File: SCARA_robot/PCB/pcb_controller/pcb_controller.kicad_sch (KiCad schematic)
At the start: 41 parts, among them IC1 LD1117-3.3V-SOT223, J1 Barrel_Jack_Switch, J10 interface, J11 Conn_01x07_Socket, J12 Encoder_A, J13 Encoder_B, J14 Encoder_C, J2 Conn_01x04_Pin_STEPPER_A, J3 interface, J4 power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

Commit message: schematic ready
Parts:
- added A2, A3: Pololu_Breakout_DRV8825, Module:Pololu_Breakout-16_15.2x20.3mm, symbol Driver_Motor:Pololu_Breakout_DRV8825
- added J15: Conn_01x04_Pin_STEPPER_B, Connector_JST:JST_XH_B4B-XH-AM_1x04_P2.50mm_Vertical, symbol Connector:Conn_01x04_Pin
- added J16: Conn_01x04_Pin_STEPPER_C, Connector_JST:JST_XH_B4B-XH-AM_1x04_P2.50mm_Vertical, symbol Connector:Conn_01x04_Pin
- added JP4, JP5, JP6: SolderJumper_2_Open, Jumper:SolderJumper-2_P1.3mm_Open_RoundedPad1.0x1.5mm, symbol Jumper:SolderJumper_2_Open
- added SW2, SW3: Microstep mode, Button_Switch_THT:SW_DIP_SPSTx03_Slide_9.78x9.8mm_W7.62mm_P2.54mm, symbol Switch:SW_DIP_x03
- added U3: PCA9548A, symbol modules:1{colon}8_i2c_mux
- JP1, JP2, JP3: footprint (none) -> Jumper:SolderJumper-3_P1.3mm_Open_RoundedPad1.0x1.5mm
- SW1: footprint (none) -> Button_Switch_THT:SW_DIP_SPSTx03_Slide_9.78x9.8mm_W7.62mm_P2.54mm
- U1: footprint PCM_Package_TO_SOT_THT_AKL:TO-220-3_Vertical -> PCM_4ms_Package_TO:TO-220-3_Horizontal
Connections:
- net +12V: now also A2.8 (VMOT), A3.8 (VMOT)
- net +3.3V: now also SW2.1, SW2.2, SW2.3, SW3.1, SW3.2, SW3.3, U3.1 (vin)
- net GNDA: now also A2.1 (GND), A2.7 (GND), A3.1 (GND), A3.7 (GND), U3.2 (gnd), U3.6 (a0), U3.7 (a1), U3.8 (a2)
- net rst_master: now also U2.4 (D2), U3.5 (rst)
- net scl_enA: now also R4.2, U3.13 (sc7); no longer R5.2
- net scl_enB: now also R6.2, U3.15 (sc6); no longer R7.2
- net scl_enC: now also R8.2, U3.17 (sc5); no longer R9.2
- net scl_master: now also R1.2, U2.14 (D22), U3.4 (scl); no longer R2.2
- net sda_enA: now also R5.2, U3.14 (sd7); no longer R4.2
- net sda_enB: now also R7.2, U3.16 (sd6); no longer R6.2
- net sda_enC: now also R9.2, U3.18 (sd5); no longer R8.2
- net sda_master: now also R2.2, U2.11 (D21), U3.3 (sda); no longer R1.2
- net baseM_rst: now reaches U2.15 (D23)
- net baseM_rst: now also A1.13 (~{RST})
- net link2_dir: now reaches U2.21 (D32)
- net link2_dir: now also A3.16 (DIR)
- net link1_dir: now reaches U2.22 (D33)
- net link1_dir: now also A2.16 (DIR)
- net baseM_step: now reaches U2.23 (D25)
- net baseM_step: now also A1.15 (STEP)
- net link1_step: now reaches U2.24 (D26)
- net link1_step: now also A2.15 (STEP)
- net link2_step: now reaches U2.25 (D27)
- net link2_step: now also A3.15 (STEP)
- net baseM_dir: now reaches U2.28 (D13)
- net baseM_dir: now also A1.16 (DIR)
- net link2_rst: now reaches U2.6 (RX2)
- net link2_rst: now also A3.13 (~{RST})
- net link1_rst: now reaches U2.7 (TX2)
- net link1_rst: now also A2.13 (~{RST})
- net at A1.14 (~{SLP}): now also JP4.2 (B)
- net at A1.2 (~{FLT}): now also JP4.1 (A)
- new net: A3.12 (M2), SW3.4
- new net: A3.11 (M1), SW3.5
- new net: A3.10 (M0), SW3.6
- new net: A2.12 (M2), SW2.4
- new net: A2.11 (M1), SW2.5
- new net: A2.10 (M0), SW2.6
- new net: A2.6 (B2), J15.1 (Pin_1)
- new net: A2.5 (B1), J15.2 (Pin_2)
- new net: A2.3 (A2), J15.3 (Pin_3)
- new net: A2.4 (A1), J15.4 (Pin_4)
- new net: A2.2 (~{FLT}), JP5.1 (A)
- new net: A2.14 (~{SLP}), JP5.2 (B)
- new net: A3.2 (~{FLT}), JP6.1 (A)
- new net: A3.14 (~{SLP}), JP6.2 (B)
- new net: A3.6 (B2), J16.1 (Pin_1)
- new net: A3.5 (B1), J16.2 (Pin_2)
- new net: A3.3 (A2), J16.3 (Pin_3)
- new net: A3.4 (A1), J16.4 (Pin_4)
- no-connect marks 5 -> 17
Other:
- moved on the sheet: A1, J2, R1, R10, R2, R4, R5, R6, R7, R8, R9, SW1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

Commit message: schematic ready
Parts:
- removed IC1: LD1117-3.3V-SOT223, PCM_Package_TO_SOT_SMD_AKL:TO-252-2_ThermalVias, symbol PCM_4ms_Regulator:LD1117-3.3V-SOT223
- added U4: LD1117S33TR_SOT223, Package_TO_SOT_SMD:SOT-223-3_TabPin2, symbol Regulator_Linear:LD1117S33TR_SOT223
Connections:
- net +3.3V: now also U4.2 (VO)
- net +5V: now also U4.3 (VI)
- net GNDA: now also U4.1 (GND)
- no-connect marks 17 -> 28
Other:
- moved on the sheet: R4, R5, R6, R7, R8, R9

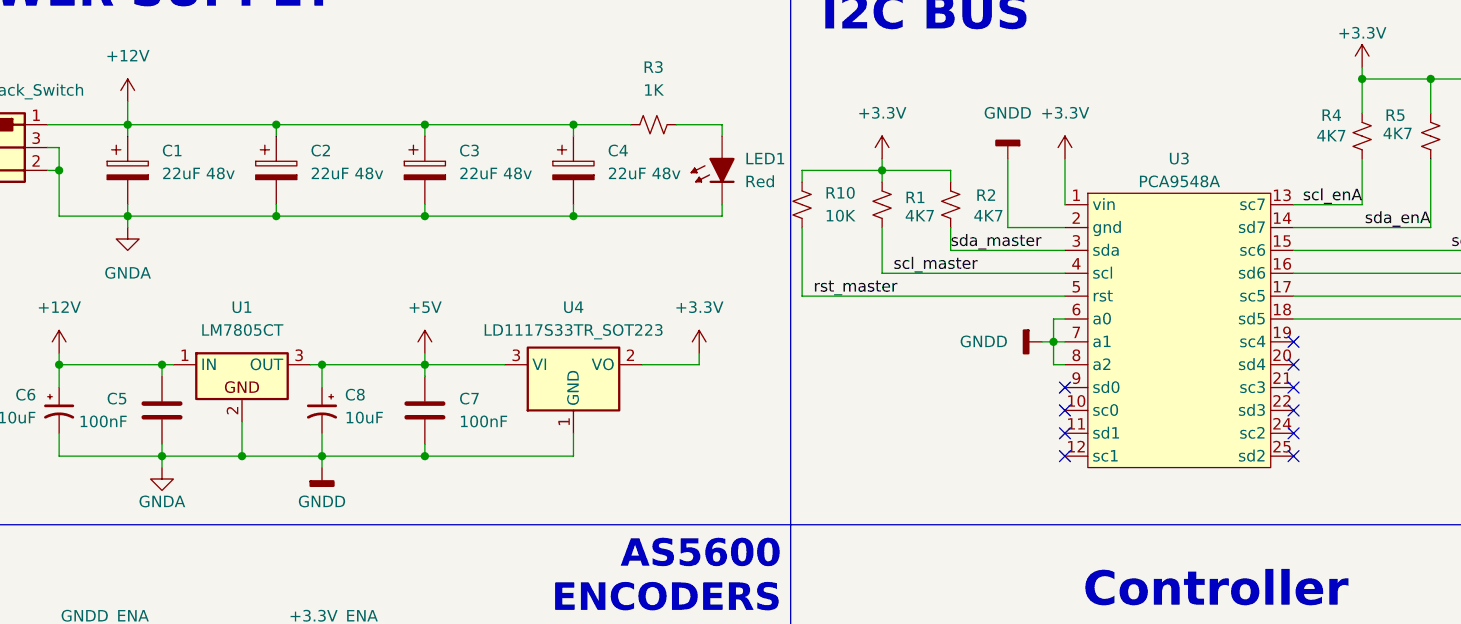
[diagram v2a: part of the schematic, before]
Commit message: schematic and footprints ready
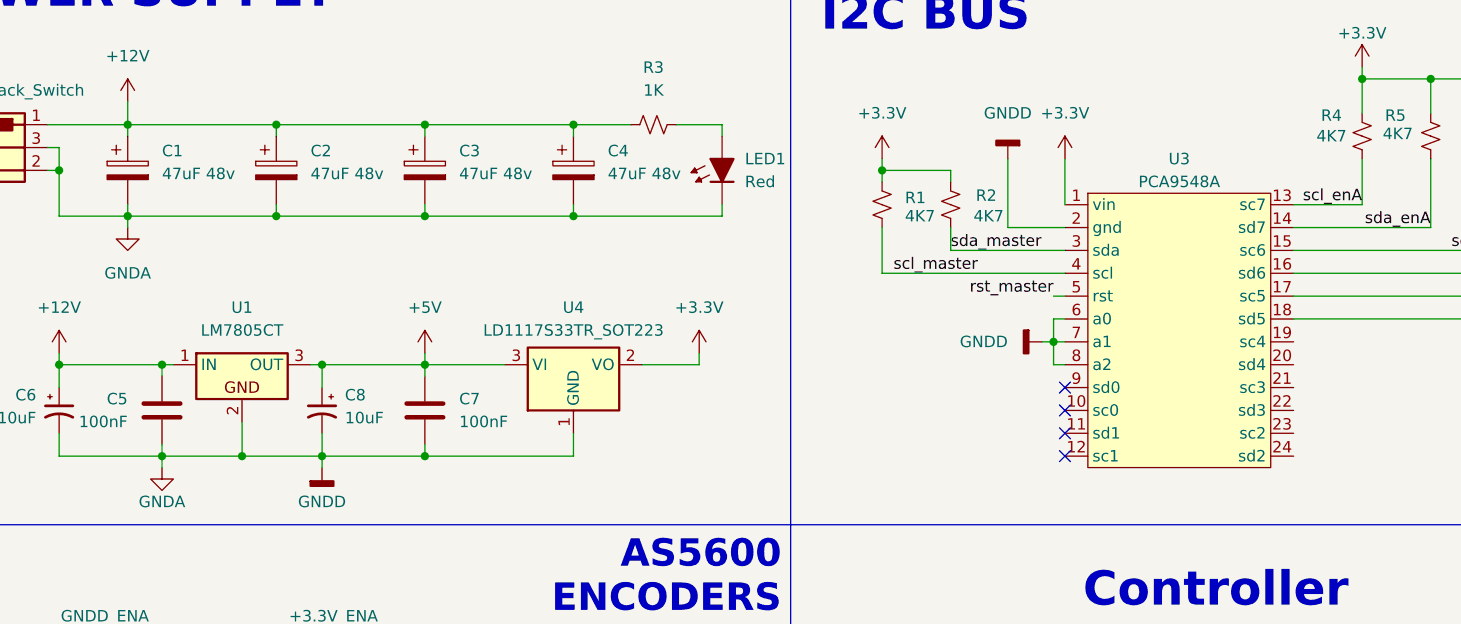
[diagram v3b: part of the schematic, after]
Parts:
- removed R10: 10K, PCM_Resistor_THT_AKL:R_Axial_DIN0204_L3.6mm_D1.6mm_P5.08mm_Horizontal, symbol Device:R_Small_US
- C1, C2, C3, C4: value 22uF 48v -> 47uF 48v
- U3: footprint (none) -> modules:TCA9548A
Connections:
- no-connect marks 28 -> 22
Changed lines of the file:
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@@
 	)
 	(no_connect
-		(at 165.1 67.31)
-	)
-	(no_connect
 		(at 245.11 35.56)
 	)
@@
 	)
 	(no_connect
-		(at 165.1 54.61)
-	)
-	(no_connect
 		(at 139.7 67.31)
 	)
@@
 	)
 	(no_connect
-		(at 165.1 62.23)
-	)
-	(no_connect
-		(at 165.1 59.69)
-	)
-	(no_connect
 		(at 143.51 104.14)
 	)
@@
 	)
 	(no_connect
-		(at 165.1 57.15)
-	)
-	(no_connect
-		(at 165.1 64.77)
-	)
-	(no_connect
 		(at 143.51 139.7)
 	)
@@
 	(wire
 		(pts
+			(xy 138.43 49.53) (xy 139.7 49.53)
+		)
+		(stroke
+			(width 0)
+			(type default)
+		)
+	)
+	(wire
+		(pts
 			(xy 27.94 67.31) (xy 39.37 67.31)
 		)
@@
 	(wire
 		(pts
-			(xy 110.49 49.53) (xy 139.7 49.53)
-		)
-		(stroke
-			(width 0)
-			(type default)
-		)
-	)
-	(wire
-		(pts
 			(xy 142.24 124.46) (xy 143.51 124.46)
 		)
@@
 	(wire
 		(pts
-			(xy 110.49 35.56) (xy 119.38 35.56)
-		)
-		(stroke
-			(width 0)
-			(type default)
-		)
-	)
-	(wire
-		(pts
 			(xy 226.06 127) (xy 226.06 132.08)
 		)
@@
 	(wire
 		(pts
-			(xy 110.49 41.91) (xy 110.49 49.53)
-		)
-		(stroke
-			(width 0)
-			(type default)
-		)
-	)
-	(wire
-		(pts
 			(xy 96.52 30.48) (xy 101.6 30.48)
 		)
@@
 	(wire
 		(pts
-			(xy 110.49 36.83) (xy 110.49 35.56)
-		)
-		(stroke
-			(width 0)
-			(type default)
-		)
-	)
-	(wire
-		(pts
 			(xy 68.58 55.88) (xy 68.58 57.15)
 		)
@@
 	)
 	(label "rst_master"
-		(at 111.76 49.53 0)
+		(at 138.43 49.53 180)
 		(effects
 			(font
 				(size 1.27 1.27)
 			)
-			(justify left bottom)
+			(justify right bottom)
 		)
 	)
@@
 			)
 		)
-		(property "Value" "22uF 48v"
+		(property "Value" "47uF 48v"
 			(at 55.88 35.9409 0)
 			(effects
@@
 			)
 		)
-		(property "Value" "22uF 48v"
+		(property "Value" "47uF 48v"
 			(at 88.9 35.9409 0)
 			(effects
@@
 	)
 	(symbol
-		(lib_id "Device:R_Small_US")
-		(at 110.49 39.37 0)
-		(unit 1)
-		(exclude_from_sim no)
-		(in_bom yes)
-		(on_board yes)
-		(dnp no)
-		(property "Reference" "R10"
-			(at 113.03 38.1 0)
-			(effects
-				(font
-					(size 1.27 1.27)
-				)
-				(justify left)
-			)
-		)
-		(property "Value" "10K"
-			(at 113.03 40.6399 0)
-			(effects
-				(font
-					(size 1.27 1.27)
-				)
-				(justify left)
-			)
-		)
-		(property "Footprint" "PCM_Resistor_THT_AKL:R_Axial_DIN0204_L3.6mm_D1.6mm_P5.08mm_Horizontal"
-			(at 110.49 39.37 0)
-			(effects
-				(font
-					(size 1.27 1.27)
-				)
-				(hide yes)
-			)
-		)
-		(property "Datasheet" "~"
-			(at 110.49 39.37 0)
-			(effects
-				(font
-					(size 1.27 1.27)
-				)
-				(hide yes)
-			)
-		)
-		(property "Description" "Resistor, small US symbol"
-			(at 110.49 39.37 0)
-			(effects
-				(font
-					(size 1.27 1.27)
-				)
-				(hide yes)
-			)
-		)
-		(pin "2"
-		)
-		(pin "1"
-		)
-		(instances
-			(project "pcb_controller"
-				(path "/d37cc98a-e228-4973-bb4e-be9654c7ae0b"
-					(reference "R10")
-					(unit 1)
-				)
-			)
-		)
-	)
-	(symbol
 		(lib_id "PCM_LED_AKL:LED_5mm")
 		(at 101.6 35.56 90)
@@
 			)
 		)
-		(property "Value" "22uF 48v"
+		(property "Value" "47uF 48v"
 			(at 39.37 35.9409 0)
 			(effects
@@
 			)
 		)
-		(property "Value" "22uF 48v"
+		(property "Value" "47uF 48v"
 			(at 72.39 35.9409 0)
 			(effects
@@
 			)
 		)
-		(property "Footprint" ""
+		(property "Footprint" "modules:TCA9548A"
 			(at 152.4 36.83 0)
 			(effects
@@
 			)
 		)
-		(property "Datasheet" ""
+		(property "Datasheet" "https://www.ti.com/lit/ds/symlink/pca9548a.pdf"
 			(at 152.4 36.83 0)
 			(effects
@@
 		(pin "6"
 		)
-		(pin "25"
+		(pin "23"
 		)
 		(pin "10"

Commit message: pcb designed phase 1
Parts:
- removed J12: Encoder_A, Connector_JST:JST_XH_B7B-XH-AM_1x07_P2.50mm_Vertical, symbol Connector:Conn_01x07_Pin
- removed J13: Encoder_B, Connector_JST:JST_XH_B7B-XH-AM_1x07_P2.50mm_Vertical, symbol Connector:Conn_01x07_Pin
- removed J14: Encoder_C, Connector_JST:JST_XH_B7B-XH-AM_1x07_P2.50mm_Vertical, symbol Connector:Conn_01x07_Pin
- removed R1, R2: 4K7, PCM_Resistor_THT_AKL:R_Axial_DIN0204_L3.6mm_D1.6mm_P5.08mm_Horizontal, symbol Device:R_Small_US
- removed SW1, SW2, SW3: Microstep mode, Button_Switch_THT:SW_DIP_SPSTx03_Slide_9.78x9.8mm_W7.62mm_P2.54mm, symbol Switch:SW_DIP_x03
- added D2: SS36, Diode_SMD:D_2114_3652Metric_Pad1.85x3.75mm_HandSolder, symbol PCM_Diode_Schottky_AKL:SS36
- added H1, H2, H3, H4: MountingHole, MountingHole:MountingHole_3.2mm_M3_ISO14580, symbol Mechanical:MountingHole
- added J17: Conn_01x02_Pin, Connector_PinSocket_2.54mm:PinSocket_1x02_P2.54mm_Vertical, symbol Connector:Conn_01x02_Pin
- added J18, J19, J20: Conn_01x04_Pin_STEPPER_C, Connector_JST:JST_XH_B4B-XH-AM_1x04_P2.50mm_Vertical, symbol Connector:Conn_01x04_Pin
- added JP10, JP11, JP12, JP13, JP14, JP15, JP7, JP8, JP9: Jumper_2_Open, PCM_Jumper_AKL:Jumper_P2.54mm_D0.7mm, symbol Jumper:Jumper_2_Open
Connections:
- net +12V: now also D2.1 (K); no longer J1.1
- net +3.3V: now also J18.1 (Pin_1), J19.1 (Pin_1), J20.1 (Pin_1), JP10.1 (A), JP11.1 (A), JP12.1 (A), JP13.1 (A), JP14.1 (A), JP15.1 (A), JP7.1 (A), JP9.1 (A)
- net +5V: now also J17.1 (Pin_1); no longer U2.30 (VIN)
- net GNDA: now also J18.2 (Pin_2), J19.2 (Pin_2), J20.2 (Pin_2)
- net scl_enA: now also J18.3 (Pin_3)
- net scl_enB: now also U3.19 (sc4), J19.3 (Pin_3); no longer U3.15 (sc6)
- net scl_enC: now also U3.23 (sc2), J20.3 (Pin_3); no longer U3.17 (sc5)
- net sda_enA: now also J18.4 (Pin_4)
- net sda_enB: now also U3.20 (sd4), J19.4 (Pin_4); no longer U3.16 (sd6)
- net sda_enC: now also U3.24 (sd2), J20.4 (Pin_4); no longer U3.18 (sd5)
- net at A3.12 (M2): now also JP15.2 (B)
- net at A3.11 (M1): now also JP14.2 (B)
- net at A3.10 (M0): now also JP13.2 (B)
- net at J2.3 (Pin_3): now also A1.4 (A1); no longer A1.3 (A2)
- net at J2.4 (Pin_4): now also A1.3 (A2); no longer A1.4 (A1)
- net at A2.12 (M2): now also JP12.2 (B)
- net at A2.11 (M1): now also JP11.2 (B)
- net at A2.10 (M0): now also JP10.2 (B)
- net at J15.3 (Pin_3): now also A2.4 (A1); no longer A2.3 (A2)
- net at J15.4 (Pin_4): now also A2.3 (A2); no longer A2.4 (A1)
- net at A1.12 (M2): now also JP9.2 (B)
- net at A1.11 (M1): now also JP8.2 (B)
- net at A1.10 (M0): now also JP7.2 (B)
- net at J16.3 (Pin_3): now also A3.4 (A1); no longer A3.3 (A2)
- net at J16.4 (Pin_4): now also A3.3 (A2); no longer A3.4 (A1)
- new net: D2.2 (A), J1.1
- new net: J17.2 (Pin_2), U2.30 (VIN)
- no-connect marks 22 -> 28
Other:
- note added: "Mounting holes"
- moved on the sheet: R4, R5, R6, R7, R8, R9, U3

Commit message: pcb designed phase 2
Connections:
- net +3.3V: now also JP8.1 (A)
- net baseM_rst: now also U2.6 (RX2); no longer U2.15 (D23)
- net link1_step: now also U2.25 (D27); no longer U2.24 (D26)
- net link2_rst: now also U2.15 (D23); no longer U2.6 (RX2)
- net link2_step: now also U2.24 (D26); no longer U2.25 (D27)
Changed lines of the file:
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@@
 	)
 	(junction
+		(at 218.44 147.32)
+		(diameter 0)
+		(color 0 0 0 0)
+	)
+	(junction
 		(at 68.58 40.64)
 		(diameter 0)
@@
 	)
 	(junction
-		(at 68.58 30.48)
+		(at 218.44 53.34)
 		(diameter 0)
 		(color 0 0 0 0)
 	)
 	(junction
-		(at 218.44 154.94)
+		(at 68.58 30.48)
 		(diameter 0)
 		(color 0 0 0 0)
@@
 	)
 	(junction
-		(at 200.66 26.67)
+		(at 218.44 154.94)
 		(diameter 0)
 		(color 0 0 0 0)
 	)
 	(junction
-		(at 85.09 40.64)
+		(at 200.66 26.67)
 		(diameter 0)
 		(color 0 0 0 0)
 	)
 	(junction
-		(at 193.04 26.67)
+		(at 85.09 40.64)
 		(diameter 0)
 		(color 0 0 0 0)
 	)
 	(junction
-		(at 33.02 97.79)
+		(at 193.04 26.67)
 		(diameter 0)
 		(color 0 0 0 0)
 	)
 	(junction
-		(at 218.44 147.32)
+		(at 33.02 97.79)
 		(diameter 0)
 		(color 0 0 0 0)
@@
 	(wire
 		(pts
+			(xy 218.44 60.96) (xy 218.44 53.34)
+		)
+		(stroke
+			(width 0)
+			(type default)
+		)
+	)
+	(wire
+		(pts
 			(xy 31.75 170.18) (xy 59.69 170.18)
 		)
@@
 	(wire
 		(pts
-			(xy 243.84 38.1) (xy 245.11 38.1)
-		)
-		(stroke
-			(width 0)
-			(type default)
-		)
-	)
-	(wire
-		(pts
-			(xy 68.58 31.75) (xy 68.58 30.48)
+			(xy 223.52 60.96) (xy 218.44 60.96)
 		)
 		(stroke
@@
 	(wire
 		(pts
-			(xy 218.44 53.34) (xy 223.52 53.34)
+			(xy 243.84 38.1) (xy 245.11 38.1)
 		)
 		(stroke
@@
 	(wire
 		(pts
-			(xy 223.52 162.56) (xy 218.44 162.56)
+			(xy 68.58 31.75) (xy 68.58 30.48)
 		)
 		(stroke
@@
 	(wire
 		(pts
-			(xy 218.44 144.78) (xy 218.44 147.32)
-		)
-		(stroke
-			(width 0)
-			(type default)
-		)
-	)
-	(wire
-		(pts
 			(xy 243.84 142.24) (xy 245.11 142.24)
 		)
@@
 	(wire
 		(pts
-			(xy 218.44 45.72) (xy 218.44 60.96)
+			(xy 218.44 45.72) (xy 218.44 53.34)
 		)
 		(stroke
@@
 	(wire
 		(pts
-			(xy 223.52 60.96) (xy 218.44 60.96)
-		)
-		(stroke
-			(width 0)
-			(type default)
-		)
-	)
-	(wire
-		(pts
 			(xy 242.57 53.34) (xy 242.57 48.26)
 		)
@@
 	(wire
 		(pts
+			(xy 218.44 147.32) (xy 223.52 147.32)
+		)
+		(stroke
+			(width 0)
+			(type default)
+		)
+	)
+	(wire
+		(pts
 			(xy 26.67 187.96) (xy 27.94 187.96)
 		)
@@
 	(wire
 		(pts
-			(xy 218.44 147.32) (xy 223.52 147.32)
-		)
-		(stroke
-			(width 0)
-			(type default)
-		)
-	)
-	(wire
-		(pts
 			(xy 200.66 35.56) (xy 200.66 66.04)
 		)
@@
 	(wire
 		(pts
-			(xy 218.44 162.56) (xy 218.44 154.94)
-		)
-		(stroke
-			(width 0)
-			(type default)
-		)
-	)
-	(wire
-		(pts
 			(xy 57.15 59.69) (xy 57.15 57.15)
 		)
@@
 	(wire
 		(pts
+			(xy 218.44 146.05) (xy 218.44 147.32)
+		)
+		(stroke
+			(width 0)
+			(type default)
+		)
+	)
+	(wire
+		(pts
 			(xy 168.91 35.56) (xy 168.91 40.64)
 		)
@@
 	(wire
 		(pts
+			(xy 218.44 162.56) (xy 218.44 154.94)
+		)
+		(stroke
+			(width 0)
+			(type default)
+		)
+	)
+	(wire
+		(pts
 			(xy 255.27 158.75) (xy 255.27 157.48)
 		)
@@
 	(wire
 		(pts
-			(xy 52.07 29.21) (xy 52.07 30.48)
+			(xy 218.44 53.34) (xy 223.52 53.34)
 		)
 		(stroke
@@
 	(wire
 		(pts
-			(xy 273.05 133.35) (xy 273.05 142.24)
+			(xy 52.07 29.21) (xy 52.07 30.48)
 		)
 		(stroke
@@
 	(wire
 		(pts
-			(xy 218.44 154.94) (xy 223.52 154.94)
+			(xy 273.05 133.35) (xy 273.05 142.24)
 		)
 		(stroke
@@
 	(wire
 		(pts
+			(xy 218.44 154.94) (xy 223.52 154.94)
+		)
+		(stroke
+			(width 0)
+			(type default)
+		)
+	)
+	(wire
+		(pts
 			(xy 175.26 152.4) (xy 175.26 153.67)
 		)
@@
 	(wire
 		(pts
-			(xy 33.02 165.1) (xy 33.02 172.72)
+			(xy 218.44 154.94) (xy 218.44 147.32)
 		)
 		(stroke
@@
 	(wire
 		(pts
-			(xy 99.06 55.88) (xy 99.06 57.15)
+			(xy 218.44 162.56) (xy 223.52 162.56)
 		)
 		(stroke
@@
 	(wire
 		(pts
-			(xy 26.67 113.03) (xy 27.94 113.03)
+			(xy 33.02 165.1) (xy 33.02 172.72)
 		)
 		(stroke
@@
 	(wire
 		(pts
-			(xy 245.11 76.2) (xy 233.68 76.2)
+			(xy 99.06 55.88) (xy 99.06 57.15)
 		)
 		(stroke
@@
 	(wire
 		(pts
-			(xy 35.56 39.37) (xy 35.56 40.64)
+			(xy 26.67 113.03) (xy 27.94 113.03)
 		)
 		(stroke
@@
 	(wire
 		(pts
-			(xy 31.75 177.8) (xy 59.69 177.8)
+			(xy 245.11 76.2) (xy 233.68 76.2)
+		)
+		(stroke
+			(width 0)
+			(type default)
+		)
+	)
+	(wire
+		(pts
+			(xy 35.56 39.37) (xy 35.56 40.64)
 		)
 		(stroke
@@
 	(wire
 		(pts
-			(xy 218.44 147.32) (xy 218.44 154.94)
+			(xy 31.75 177.8) (xy 59.69 177.8)
 		)
 		(stroke
@@
 		)
 	)
+	(label "link2_step"
+		(at 175.26 132.08 0)
+		(effects
+			(font
+				(size 1.27 1.27)
+			)
+			(justify left bottom)
+		)
+	)
 	(label "scl_enB"
 		(at 85.09 138.43 0)
@@
 		)
 	)
-	(label "link2_rst"
-		(at 175.26 116.84 0)
-		(effects
-			(font
-				(size 1.27 1.27)
-			)
-			(justify left bottom)
-		)
-	)
 	(label "scl_encoderA"
 		(at 43.18 102.87 0)
@@
 		)
 	)
+	(label "baseM_rst"
+		(at 175.26 116.84 0)
+		(effects
+			(font
+				(size 1.27 1.27)
+			)
+			(justify left bottom)
+		)
+	)
+	(label "link1_step"
+		(at 175.26 134.62 0)
+		(effects
+			(font
+				(size 1.27 1.27)
+			)
+			(justify left bottom)
+		)
+	)
+	(label "link2_rst"
+		(at 175.26 127 0)
+		(effects
+			(font
+				(size 1.27 1.27)
+			)
+			(justify left bottom)
+		)
+	)
 	(label "scl_enB"
 		(at 185.42 55.88 180)
@@
 		)
 	)
-	(label "baseM_rst"
-		(at 175.26 127 0)
-		(effects
-			(font
-				(size 1.27 1.27)
-			)
-			(justify left bottom)
-		)
-	)
 	(label "sda_encoderC"
 		(at 43.18 180.34 0)
@@
 		)
 	)
-	(label "link2_step"
-		(at 175.26 134.62 0)
-		(effects
-			(font
-				(size 1.27 1.27)
-			)
-			(justify left bottom)
-		)
-	)
 	(label "dirC"
 		(at 43.18 175.26 0)
@@
 		)
 	)
-	(label "link1_step"
-		(at 175.26 132.08 0)
-		(effects
-			(font
-				(size 1.27 1.27)
-			)
-			(justify left bottom)
-		)
-	)
 	(label "baseM_rst"
 		(at 243.84 27.94 180)
@@
 	(symbol
 		(lib_id "power:+3.3V")
-		(at 218.44 144.78 0)
+		(at 218.44 146.05 0)
 		(unit 1)
 		(exclude_from_sim no)
@@
 		(fields_autoplaced yes)
 		(property "Reference" "#PWR038"
-			(at 218.44 148.59 0)
+			(at 218.44 149.86 0)
 			(effects
 				(font
@@
 		)
 		(property "Value" "+3.3V"
-			(at 218.44 139.7 0)
+			(at 218.44 140.97 0)
 			(effects
 				(font
@@
 		)
 		(property "Footprint" ""
-			(at 218.44 144.78 0)
+			(at 218.44 146.05 0)
 			(effects
 				(font
@@
 		)
 		(property "Datasheet" ""
-			(at 218.44 144.78 0)
+			(at 218.44 146.05 0)
 			(effects
 				(font
@@
 		)
 		(property "Description" "Power symbol creates a global label with name \"+3.3V\""
-			(at 218.44 144.78 0)
+			(at 218.44 146.05 0)
 			(effects
 				(font
